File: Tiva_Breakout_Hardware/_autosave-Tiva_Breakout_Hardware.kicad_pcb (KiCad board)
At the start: 2 copper layers, 139.8 x 79.5 mm, 6 parts, among them U1 TM4C129E_Launchpad

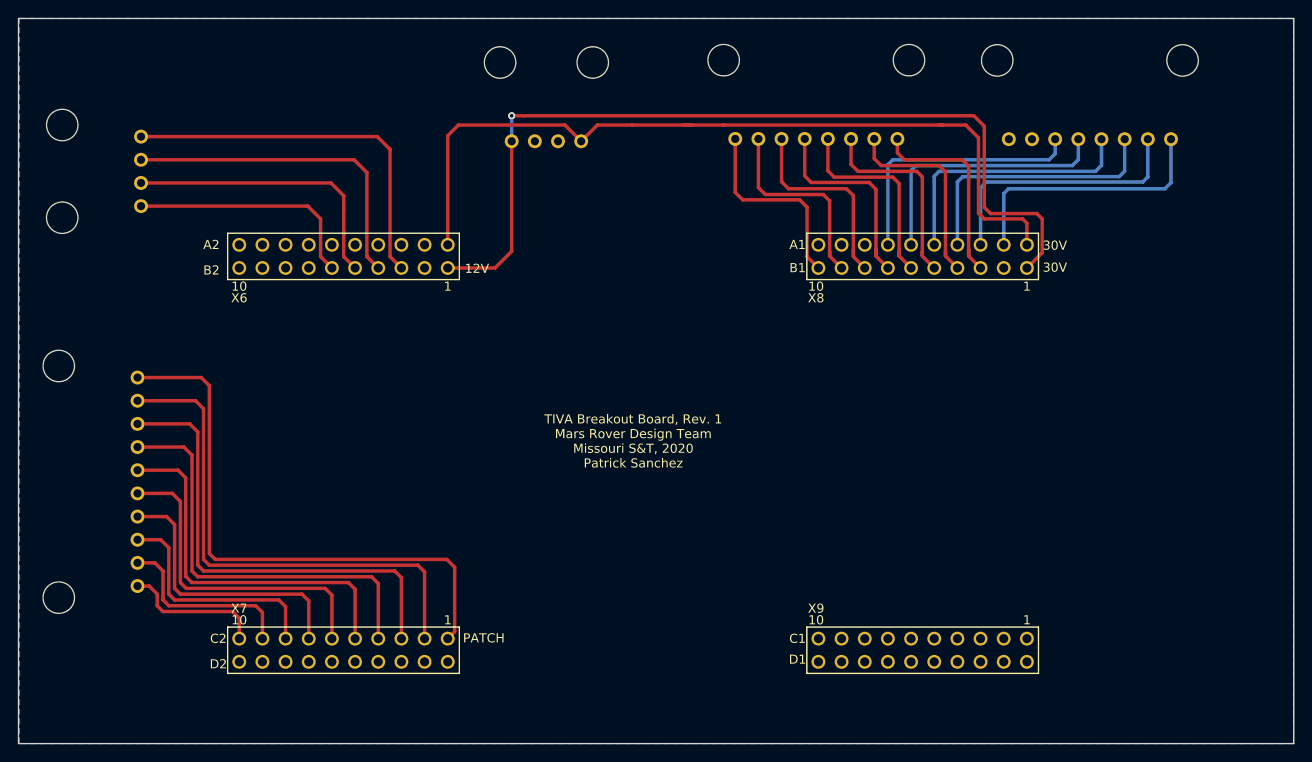
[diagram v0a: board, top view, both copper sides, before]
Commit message: In process of changing layout for smaller board
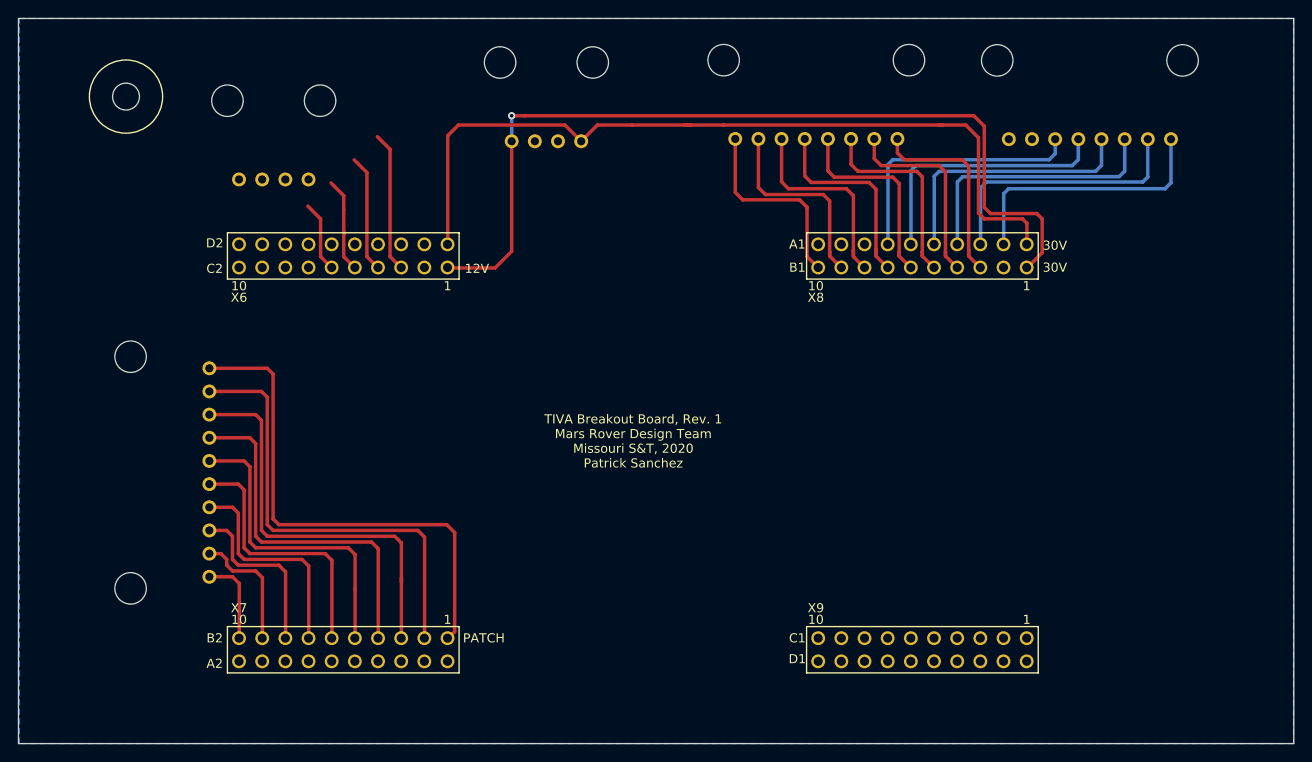
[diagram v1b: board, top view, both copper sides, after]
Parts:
- added REF**: 4_40_Hole, MRDT_Drill_Holes:4_40_Hole_Corner, F.Cu at (92.7, 83.4)
- moved U1 89.2 mm to (107.4, 131.2), turned to 0 degrees
- moved 12V_B2 14.6 mm to (104.9, 88.5), turned to 180 degrees
- moved ConnPCH_C2 7.94 mm to (97.8, 120.7)
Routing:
- net Net-(12V_B2-Pad1): track 41.4 -> 15.5 mm
- net Net-(12V_B2-Pad2): track 36.3 -> 13.0 mm
- net Net-(12V_B2-Pad3): track 31.5 -> 10.7 mm
- net Net-(12V_B2-Pad4): track 26.2 -> 7.88 mm
- net Net-(ConnPCH_C2-Pad2): track 56.2 -> 49.5 mm
- net Net-(ConnPCH_C2-Pad8): track 25.8 -> 19.0 mm
- net Net-(ConnPCH_C2-Pad6): track 35.9 -> 29.2 mm
- net Net-(ConnPCH_C2-Pad5): track 41.0 -> 34.3 mm
- net Net-(ConnPCH_C2-Pad4): track 46.1 -> 39.4 mm
- net Net-(ConnPCH_C2-Pad7): track 30.8 -> 24.1 mm
- net Net-(ConnPCH_C2-Pad9): track 20.7 -> 14.0 mm
- net Net-(ConnPCH_C2-Pad1): track 62.3 -> 55.6 mm
- net Net-(ConnPCH_C2-Pad3): track 51.2 -> 44.9 mm
- net Net-(ConnPCH_C2-Pad10): track 15.6 -> 9.63 mm
